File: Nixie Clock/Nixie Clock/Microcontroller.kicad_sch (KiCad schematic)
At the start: 17 parts, among them J2 Conn_01x05_Male, SW1 1825910-2, U10 PIC16F15325-I/P, Y1 12.288MHz

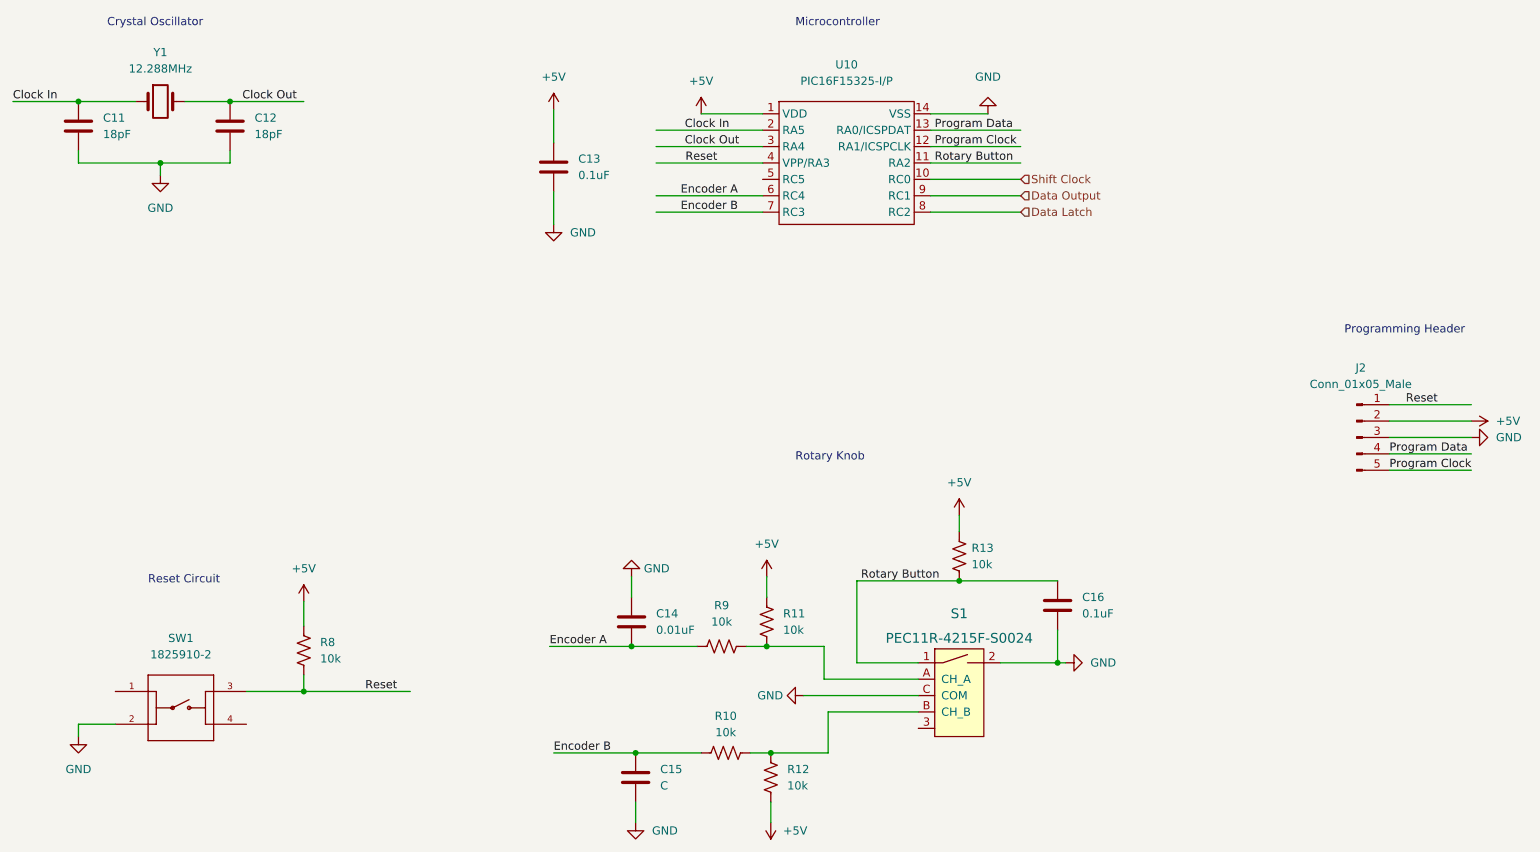
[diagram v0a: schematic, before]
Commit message: Need to add footprints for passives
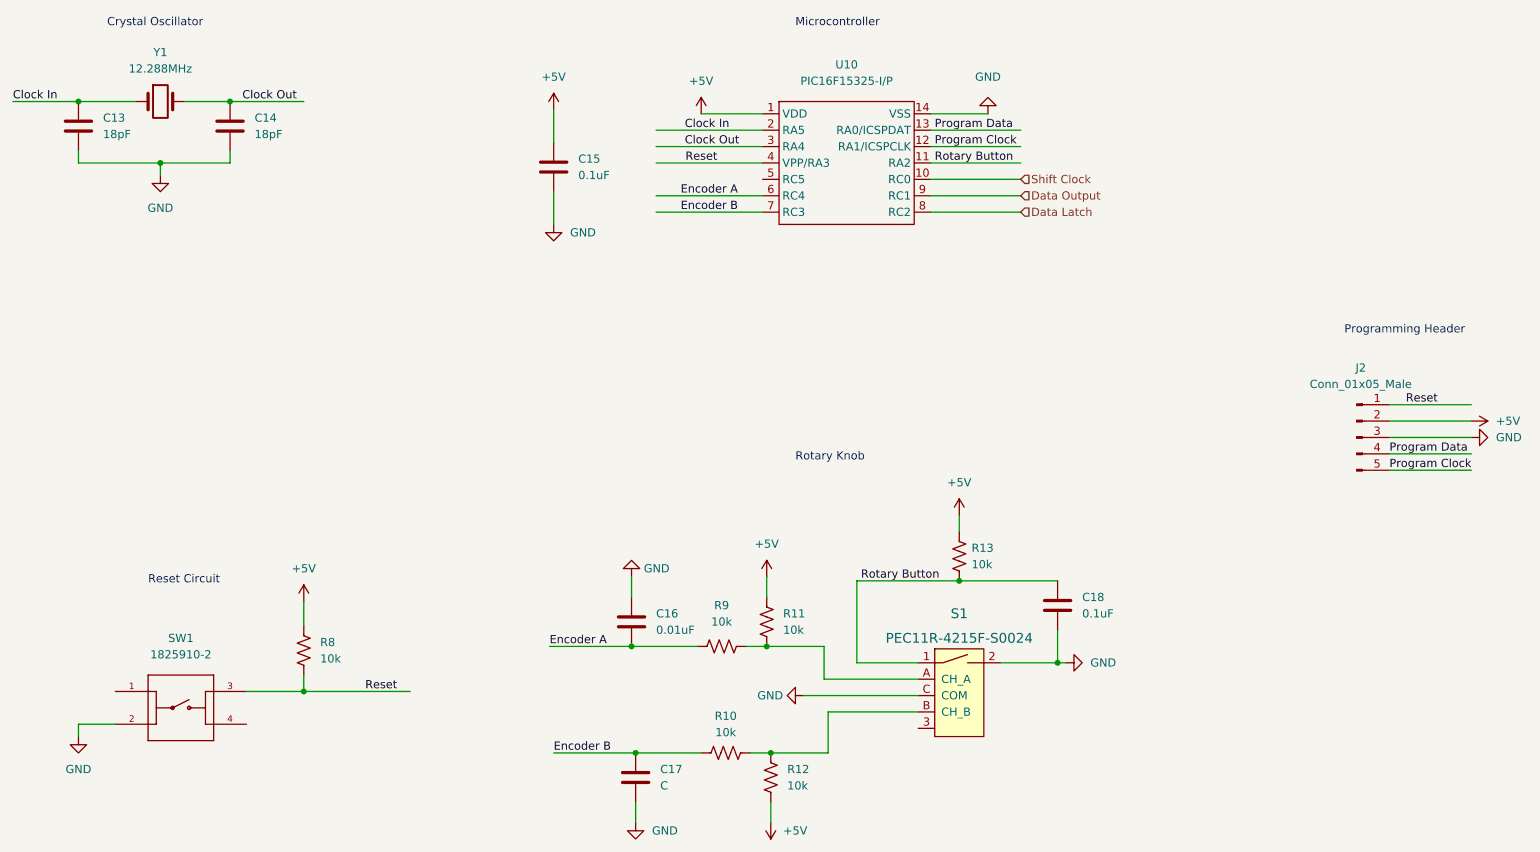
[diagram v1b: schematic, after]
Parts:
- SW1: footprint TE_1825910-2 -> 1825910-2:TE_1825910-2
- renumbered C11 to C13, C12 to C14, C13 to C15, C14 to C16, C15 to C17, C16 to C18
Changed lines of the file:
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@@
   (symbol (lib_id "power:GND") (at 127 131.445 180) (unit 1)
     (in_bom yes) (on_board yes) (fields_autoplaced)
-    (property "Reference" "#PWR050" (id 0) (at 127 125.095 0)
+    (property "Reference" "#PWR056" (id 0) (at 127 125.095 0)
       (effects (font (size 1.27 1.27)) hide)
     )
@@
   (symbol (lib_id "power:GND") (at 257.175 109.855 90) (unit 1)
     (in_bom yes) (on_board yes) (fields_autoplaced)
-    (property "Reference" "#PWR060" (id 0) (at 263.525 109.855 0)
+    (property "Reference" "#PWR066" (id 0) (at 263.525 109.855 0)
       (effects (font (size 1.27 1.27)) hide)
     )
@@
   (symbol (lib_id "power:+5V") (at 148.59 169.545 180) (unit 1)
     (in_bom yes) (on_board yes) (fields_autoplaced)
-    (property "Reference" "#PWR054" (id 0) (at 148.59 165.735 0)
+    (property "Reference" "#PWR060" (id 0) (at 148.59 165.735 0)
       (effects (font (size 1.27 1.27)) hide)
     )
@@
   (symbol (lib_id "power:GND") (at 127.635 169.545 0) (unit 1)
     (in_bom yes) (on_board yes) (fields_autoplaced)
-    (property "Reference" "#PWR051" (id 0) (at 127.635 175.895 0)
+    (property "Reference" "#PWR057" (id 0) (at 127.635 175.895 0)
       (effects (font (size 1.27 1.27)) hide)
     )
@@
   (symbol (lib_id "power:GND") (at 182.245 59.69 180) (unit 1)
     (in_bom yes) (on_board yes) (fields_autoplaced)
-    (property "Reference" "#PWR057" (id 0) (at 182.245 53.34 0)
+    (property "Reference" "#PWR063" (id 0) (at 182.245 53.34 0)
       (effects (font (size 1.27 1.27)) hide)
     )
@@
   (symbol (lib_id "Device:C") (at 114.935 67.945 0) (unit 1)
     (in_bom yes) (on_board yes) (fields_autoplaced)
-    (property "Reference" "C13" (id 0) (at 118.745 66.6749 0)
+    (property "Reference" "C15" (id 0) (at 118.745 66.6749 0)
       (effects (font (size 1.27 1.27)) (justify left))
     )
@@
   (symbol (lib_id "Device:C") (at 64.77 61.595 0) (unit 1)
     (in_bom yes) (on_board yes) (fields_autoplaced)
-    (property "Reference" "C12" (id 0) (at 68.58 60.3249 0)
+    (property "Reference" "C14" (id 0) (at 68.58 60.3249 0)
       (effects (font (size 1.27 1.27)) (justify left))
     )
@@
   (symbol (lib_id "power:+5V") (at 147.955 131.445 0) (unit 1)
     (in_bom yes) (on_board yes) (fields_autoplaced)
-    (property "Reference" "#PWR053" (id 0) (at 147.955 135.255 0)
+    (property "Reference" "#PWR059" (id 0) (at 147.955 135.255 0)
       (effects (font (size 1.27 1.27)) hide)
     )
@@
   (symbol (lib_id "power:+5V") (at 76.2 135.255 0) (unit 1)
     (in_bom yes) (on_board yes) (fields_autoplaced)
-    (property "Reference" "#PWR047" (id 0) (at 76.2 139.065 0)
+    (property "Reference" "#PWR053" (id 0) (at 76.2 139.065 0)
       (effects (font (size 1.27 1.27)) hide)
     )
@@
   (symbol (lib_id "power:+5V") (at 114.935 59.055 0) (unit 1)
     (in_bom yes) (on_board yes) (fields_autoplaced)
-    (property "Reference" "#PWR048" (id 0) (at 114.935 62.865 0)
+    (property "Reference" "#PWR054" (id 0) (at 114.935 62.865 0)
       (effects (font (size 1.27 1.27)) hide)
     )
@@
   (symbol (lib_id "power:+5V") (at 257.175 107.315 270) (unit 1)
     (in_bom yes) (on_board yes) (fields_autoplaced)
-    (property "Reference" "#PWR059" (id 0) (at 253.365 107.315 0)
+    (property "Reference" "#PWR065" (id 0) (at 253.365 107.315 0)
       (effects (font (size 1.27 1.27)) hide)
     )
@@
   (symbol (lib_id "power:GND") (at 41.275 156.21 0) (unit 1)
     (in_bom yes) (on_board yes) (fields_autoplaced)
-    (property "Reference" "#PWR045" (id 0) (at 41.275 162.56 0)
+    (property "Reference" "#PWR051" (id 0) (at 41.275 162.56 0)
       (effects (font (size 1.27 1.27)) hide)
     )
@@
   (symbol (lib_id "power:+5V") (at 137.795 59.69 0) (unit 1)
     (in_bom yes) (on_board yes) (fields_autoplaced)
-    (property "Reference" "#PWR052" (id 0) (at 137.795 63.5 0)
+    (property "Reference" "#PWR058" (id 0) (at 137.795 63.5 0)
       (effects (font (size 1.27 1.27)) hide)
     )
@@
   (symbol (lib_id "Device:C") (at 193.04 135.89 0) (unit 1)
     (in_bom yes) (on_board yes) (fields_autoplaced)
-    (property "Reference" "C16" (id 0) (at 196.85 134.6199 0)
+    (property "Reference" "C18" (id 0) (at 196.85 134.6199 0)
       (effects (font (size 1.27 1.27)) (justify left))
     )
@@
   (symbol (lib_id "power:GND") (at 153.67 149.86 270) (unit 1)
     (in_bom yes) (on_board yes) (fields_autoplaced)
-    (property "Reference" "#PWR055" (id 0) (at 147.32 149.86 0)
+    (property "Reference" "#PWR061" (id 0) (at 147.32 149.86 0)
       (effects (font (size 1.27 1.27)) hide)
     )
@@
   (symbol (lib_id "Device:C") (at 127 138.43 0) (unit 1)
     (in_bom yes) (on_board yes) (fields_autoplaced)
-    (property "Reference" "C14" (id 0) (at 130.81 137.1599 0)
+    (property "Reference" "C16" (id 0) (at 130.81 137.1599 0)
       (effects (font (size 1.27 1.27)) (justify left))
     )
@@
   (symbol (lib_id "power:GND") (at 194.31 144.78 90) (unit 1)
     (in_bom yes) (on_board yes) (fields_autoplaced)
-    (property "Reference" "#PWR058" (id 0) (at 200.66 144.78 0)
+    (property "Reference" "#PWR064" (id 0) (at 200.66 144.78 0)
       (effects (font (size 1.27 1.27)) hide)
     )
@@
   (symbol (lib_id "power:+5V") (at 177.8 121.92 0) (unit 1)
     (in_bom yes) (on_board yes) (fields_autoplaced)
-    (property "Reference" "#PWR056" (id 0) (at 177.8 125.73 0)
+    (property "Reference" "#PWR062" (id 0) (at 177.8 125.73 0)
       (effects (font (size 1.27 1.27)) hide)
     )
@@
   (symbol (lib_id "power:GND") (at 53.975 69.215 0) (unit 1)
     (in_bom yes) (on_board yes) (fields_autoplaced)
-    (property "Reference" "#PWR046" (id 0) (at 53.975 75.565 0)
+    (property "Reference" "#PWR052" (id 0) (at 53.975 75.565 0)
       (effects (font (size 1.27 1.27)) hide)
     )
@@
   (symbol (lib_id "power:GND") (at 114.935 76.835 0) (unit 1)
     (in_bom yes) (on_board yes) (fields_autoplaced)
-    (property "Reference" "#PWR049" (id 0) (at 114.935 83.185 0)
+    (property "Reference" "#PWR055" (id 0) (at 114.935 83.185 0)
       (effects (font (size 1.27 1.27)) hide)
     )
@@
     (property "Reference" "SW1" (id 0) (at 57.15 140.97 0))
     (property "Value" "1825910-2" (id 1) (at 57.15 143.51 0))
-    (property "Footprint" "TE_1825910-2" (id 2) (at 57.15 151.765 0)
+    (property "Footprint" "1825910-2:TE_1825910-2" (id 2) (at 57.15 151.765 0)
       (effects (font (size 1.27 1.27)) (justify left bottom) hide)
     )
@@
   (symbol (lib_id "Device:C") (at 127.635 162.56 0) (unit 1)
     (in_bom yes) (on_board yes) (fields_autoplaced)
-    (property "Reference" "C15" (id 0) (at 131.445 161.2899 0)
+    (property "Reference" "C17" (id 0) (at 131.445 161.2899 0)
       (effects (font (size 1.27 1.27)) (justify left))
     )
@@
   (symbol (lib_id "Device:C") (at 41.275 61.595 0) (unit 1)
     (in_bom yes) (on_board yes) (fields_autoplaced)
-    (property "Reference" "C11" (id 0) (at 45.085 60.3249 0)
-      (effects (font (size 1.27 1.27)) (justify left))
-    )
+    (property "Reference" "C13" (id 0) (at 45.085 60.3249 0)
+      (effects (font (size 1.27 1.27)) (justify left))
+    )

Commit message: Started Routing
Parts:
- C13, C14: footprint (none) -> Capacitor_THT:C_Rect_L7.0mm_W2.5mm_P5.00mm
- C15, C18: footprint (none) -> Capacitor_THT:C_Rect_L7.0mm_W3.5mm_P5.00mm
- C16: footprint (none) -> Capacitor_THT:C_Disc_D12.0mm_W4.4mm_P7.75mm
- C17: value C -> 0.01uF; footprint (none) -> Capacitor_THT:C_Disc_D12.0mm_W4.4mm_P7.75mm
- J2: footprint (none) -> Connector_PinHeader_2.54mm:PinHeader_1x05_P2.54mm_Vertical
- R10, R11, R12, R13, R8, R9: footprint (none) -> Resistor_THT:R_Axial_DIN0207_L6.3mm_D2.5mm_P10.16mm_Horizontal
- Y1: footprint (none) -> Crystal:Crystal_HC49-4H_Vertical
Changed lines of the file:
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@@
     (property "Reference" "R10" (id 0) (at 141.605 153.035 90))
     (property "Value" "10k" (id 1) (at 141.605 155.575 90))
-    (property "Footprint" "" (id 2) (at 141.859 157.734 90)
+    (property "Footprint" "Resistor_THT:R_Axial_DIN0207_L6.3mm_D2.5mm_P10.16mm_Horizontal" (id 2) (at 141.859 157.734 90)
       (effects (font (size 1.27 1.27)) hide)
     )
@@
       (effects (font (size 1.27 1.27)) (justify left))
     )
-    (property "Footprint" "" (id 2) (at 115.9002 71.755 0)
+    (property "Footprint" "Capacitor_THT:C_Rect_L7.0mm_W3.5mm_P5.00mm" (id 2) (at 115.9002 71.755 0)
       (effects (font (size 1.27 1.27)) hide)
     )
@@
       (effects (font (size 1.27 1.27)) (justify left))
     )
-    (property "Footprint" "" (id 2) (at 65.7352 65.405 0)
+    (property "Footprint" "Capacitor_THT:C_Rect_L7.0mm_W2.5mm_P5.00mm" (id 2) (at 65.7352 65.405 0)
       (effects (font (size 1.27 1.27)) hide)
     )
@@
       (effects (font (size 1.27 1.27)) (justify left))
     )
-    (property "Footprint" "" (id 2) (at 77.216 143.129 90)
+    (property "Footprint" "Resistor_THT:R_Axial_DIN0207_L6.3mm_D2.5mm_P10.16mm_Horizontal" (id 2) (at 77.216 143.129 90)
       (effects (font (size 1.27 1.27)) hide)
     )
@@
     (property "Reference" "R9" (id 0) (at 140.97 135.89 90))
     (property "Value" "10k" (id 1) (at 140.97 138.43 90))
-    (property "Footprint" "" (id 2) (at 141.224 141.224 90)
+    (property "Footprint" "Resistor_THT:R_Axial_DIN0207_L6.3mm_D2.5mm_P10.16mm_Horizontal" (id 2) (at 141.224 141.224 90)
       (effects (font (size 1.27 1.27)) hide)
     )
@@
       (effects (font (size 1.27 1.27)) (justify left))
     )
-    (property "Footprint" "" (id 2) (at 194.0052 139.7 0)
+    (property "Footprint" "Capacitor_THT:C_Rect_L7.0mm_W3.5mm_P5.00mm" (id 2) (at 194.0052 139.7 0)
       (effects (font (size 1.27 1.27)) hide)
     )
@@
       (effects (font (size 1.27 1.27)) (justify left))
     )
-    (property "Footprint" "" (id 2) (at 178.816 128.524 90)
+    (property "Footprint" "Resistor_THT:R_Axial_DIN0207_L6.3mm_D2.5mm_P10.16mm_Horizontal" (id 2) (at 178.816 128.524 90)
       (effects (font (size 1.27 1.27)) hide)
     )
@@
       (effects (font (size 1.27 1.27)) (justify left))
     )
-    (property "Footprint" "" (id 2) (at 127.9652 142.24 0)
+    (property "Footprint" "Capacitor_THT:C_Disc_D12.0mm_W4.4mm_P7.75mm" (id 2) (at 127.9652 142.24 0)
       (effects (font (size 1.27 1.27)) hide)
     )
@@
     (property "Reference" "J2" (id 0) (at 240.03 99.06 0))
     (property "Value" "Conn_01x05_Male" (id 1) (at 240.03 101.6 0))
-    (property "Footprint" "" (id 2) (at 239.395 109.855 0)
+    (property "Footprint" "Connector_PinHeader_2.54mm:PinHeader_1x05_P2.54mm_Vertical" (id 2) (at 239.395 109.855 0)
       (effects (font (size 1.27 1.27)) hide)
     )
@@
       (effects (font (size 1.27 1.27)) (justify left))
     )
-    (property "Footprint" "" (id 2) (at 148.971 138.684 90)
+    (property "Footprint" "Resistor_THT:R_Axial_DIN0207_L6.3mm_D2.5mm_P10.16mm_Horizontal" (id 2) (at 148.971 138.684 90)
       (effects (font (size 1.27 1.27)) hide)
     )
@@
     (property "Reference" "Y1" (id 0) (at 53.975 50.165 0))
     (property "Value" "12.288MHz" (id 1) (at 53.975 52.705 0))
-    (property "Footprint" "" (id 2) (at 53.975 57.785 0)
+    (property "Footprint" "Crystal:Crystal_HC49-4H_Vertical" (id 2) (at 53.975 57.785 0)
       (effects (font (size 1.27 1.27)) hide)
     )
@@
       (effects (font (size 1.27 1.27)) (justify left))
     )
-    (property "Value" "C" (id 1) (at 131.445 163.8299 0)
-      (effects (font (size 1.27 1.27)) (justify left))
-    )
-    (property "Footprint" "" (id 2) (at 128.6002 166.37 0)
+    (property "Value" "0.01uF" (id 1) (at 131.445 163.8299 0)
+      (effects (font (size 1.27 1.27)) (justify left))
+    )
+    (property "Footprint" "Capacitor_THT:C_Disc_D12.0mm_W4.4mm_P7.75mm" (id 2) (at 128.6002 166.37 0)
       (effects (font (size 1.27 1.27)) hide)
     )
@@
       (effects (font (size 1.27 1.27)) (justify left))
     )
-    (property "Footprint" "" (id 2) (at 149.606 162.814 90)
+    (property "Footprint" "Resistor_THT:R_Axial_DIN0207_L6.3mm_D2.5mm_P10.16mm_Horizontal" (id 2) (at 149.606 162.814 90)
       (effects (font (size 1.27 1.27)) hide)
     )
@@
       (effects (font (size 1.27 1.27)) (justify left))
     )
-    (property "Footprint" "" (id 2) (at 42.2402 65.405 0)
-      (effects (font (size 1.27 1.27)) hide)
-    )
+    (property "Footprint" "Capacitor_THT:C_Rect_L7.0mm_W2.5mm_P5.00mm" (id 2) (at 42.2402 65.405 0)
+      (effects (font (size 1.27 1.27)) hide)
+    )

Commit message: Nixie
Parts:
- removed J2: Conn_01x05_Male, Connector_PinHeader_2.54mm:PinHeader_1x05_P2.54mm_Vertical, symbol Connector:Conn_01x05_Male
- C13, C14: value 18pF -> (none); footprint Capacitor_THT:C_Rect_L7.0mm_W2.5mm_P5.00mm -> (none)
- C15, C18: value 0.1uF -> (none); footprint Capacitor_THT:C_Rect_L7.0mm_W3.5mm_P5.00mm -> (none)
- C16, C17: value 0.01uF -> (none); footprint Capacitor_THT:C_Disc_D12.0mm_W4.4mm_P7.75mm -> (none)
- R10, R11, R12, R13: footprint Resistor_THT:R_Axial_DIN0207_L6.3mm_D2.5mm_P10.16mm_Horizontal -> Resistor_THT:R_Axial_DIN0309_L9.0mm_D3.2mm_P12.70mm_Horizontal
- R8, R9: value 10k -> (none); footprint Resistor_THT:R_Axial_DIN0207_L6.3mm_D2.5mm_P10.16mm_Horizontal -> (none)
- S1: value PEC11R-4215F-S0024 -> (none); footprint digikey-footprints:Rotary_Encoder_Switched_PEC11R -> (none)
- Y1: value 12.288MHz -> (none); footprint Crystal:Crystal_HC49-4H_Vertical -> (none)
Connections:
- net +5V: now also R11.2, R12.1, R13.2; no longer R11.1, R12.2, R13.1
- net Rotary Button: now also R13.1; no longer R13.2
- net at R10.2, S1.B (CH_B): now also R12.2; no longer R12.1
- net at R9.2, S1.A (CH_A): now also R11.1; no longer R11.2
- net Program Clock: no longer names the net of U10.12 (RA1/ICSPCLK)
- net Program Data: no longer names the net of U10.13 (RA0/ICSPDAT)
- no-connect marks 0 -> 3
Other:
- note removed: "Programming Header"
- moved on the sheet: U10
